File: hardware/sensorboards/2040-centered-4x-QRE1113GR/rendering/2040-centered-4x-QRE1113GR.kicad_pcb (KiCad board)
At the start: 2 copper layers, 174.6 x 52 mm, 44 parts, among them J1 Conn_01x10_Male, U1 QRE1113GR, U2 QRE1113GR, U3 QRE1113GR, U4 QRE1113GR

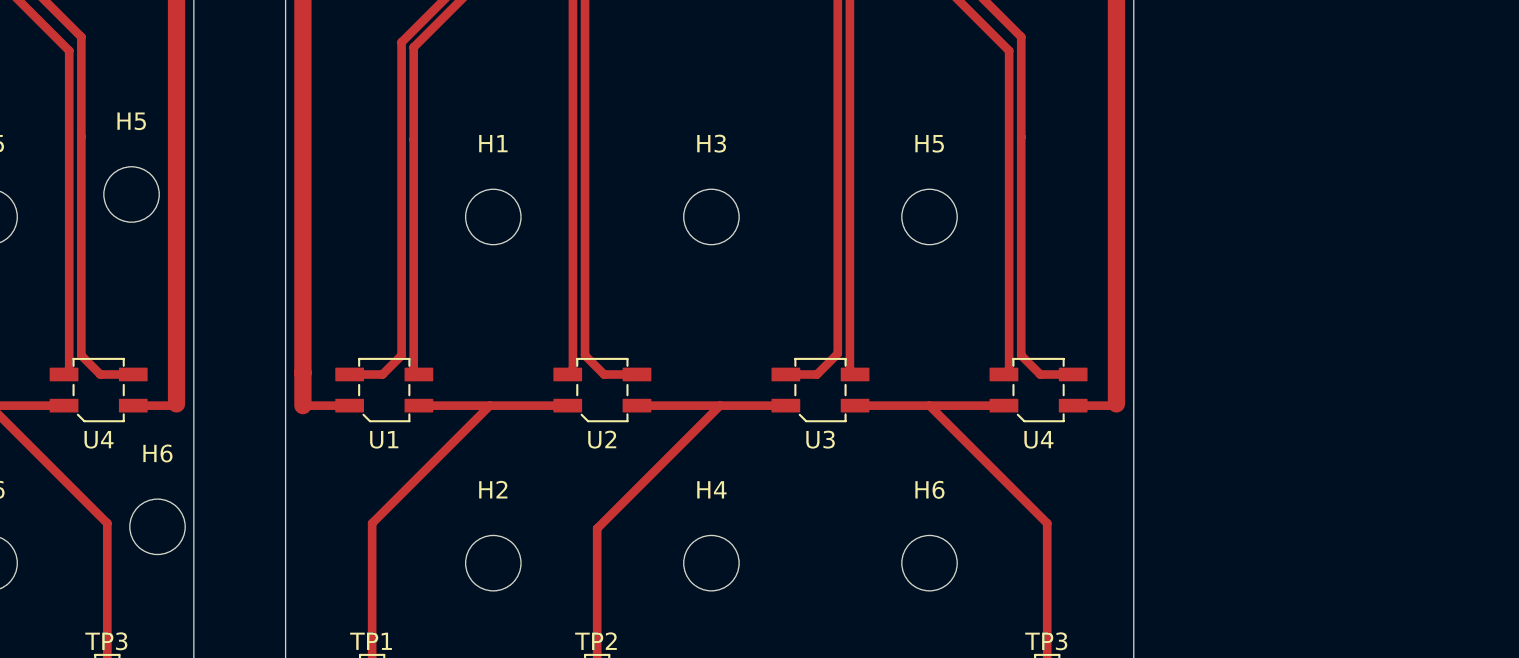
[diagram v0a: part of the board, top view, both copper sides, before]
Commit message: positioned screen and extrusions
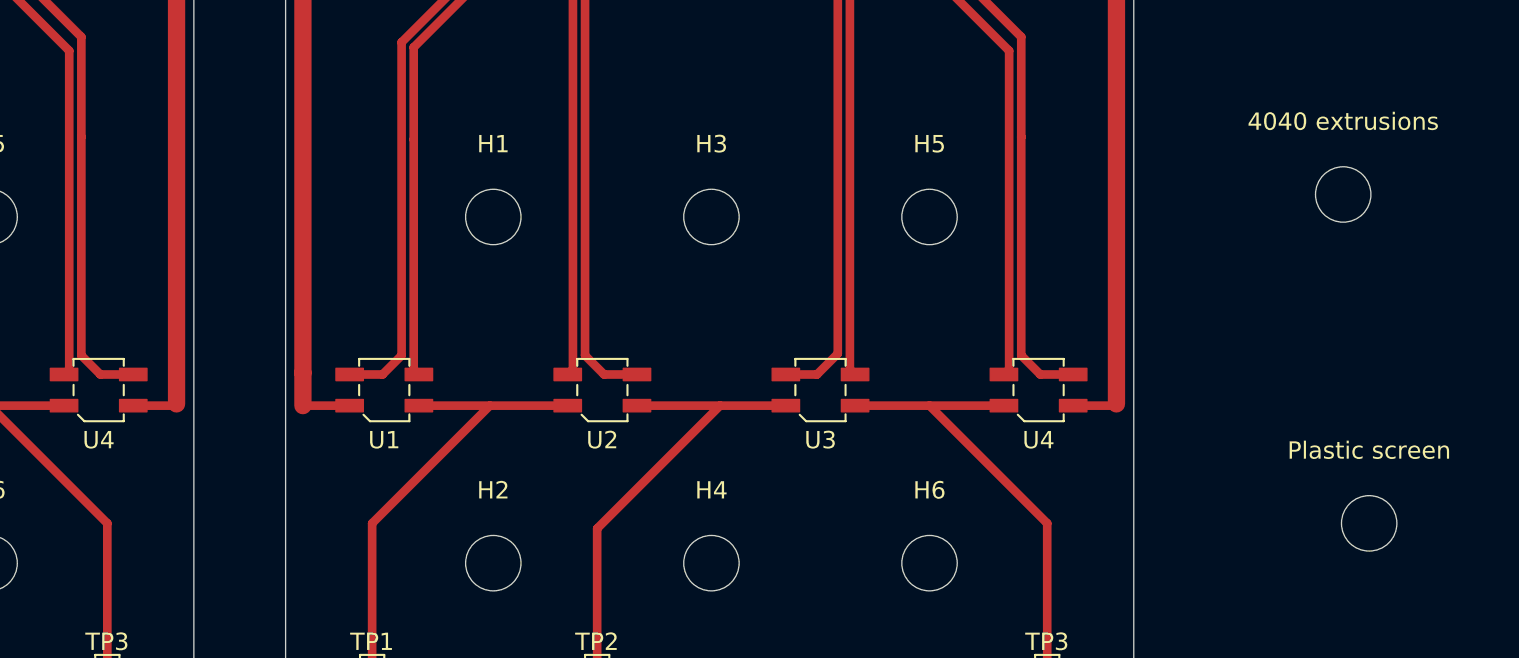
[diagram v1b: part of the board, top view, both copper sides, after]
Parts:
- 4040 extrusions: renamed from H5
- Plastic screen: renamed from H6
- moved Plastic screen 70.0 mm to (247.0, 100.0)
- moved 4040 extrusions 70.0 mm to (245.5, 81.0)
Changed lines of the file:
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@@
   )
   (footprint "Mounting_Holes:MountingHole_3.2mm_M3" (layer "F.Cu")
-    (at 177 100.2)
-    (descr "Mounting Hole 3.2mm, no annular, M3")
-    (tags "mounting hole 3.2mm no annular m3")
-    (property "Sheetfile" "2040-centered-4x-QRE1113GR.kicad_sch")
-    (property "Sheetname" "")
-    (attr exclude_from_pos_files)
-    (fp_text reference "H6" (at 0 -4.2) (layer "F.SilkS")
-      (effects (font (size 1 1) (thickness 0.15)))
-    )
-    (fp_text value "MountingHole" (at 0 4.2) (layer "F.Fab")
-      (effects (font (size 1 1) (thickness 0.15)))
-    )
-    (fp_text user "${REFERENCE}" (at 0 0) (layer "F.Fab")
+    (at 247 100)
+    (descr "Mounting Hole 3.2mm, no annular, M3")
+    (tags "mounting hole 3.2mm no annular m3")
+    (property "Sheetfile" "2040-centered-4x-QRE1113GR.kicad_sch")
+    (property "Sheetname" "")
+    (attr exclude_from_pos_files)
+    (fp_text reference "Plastic screen" (at 0 -4.2) (layer "F.SilkS")
+      (effects (font (size 1 1) (thickness 0.15)))
+    )
+    (fp_text value "MountingHole" (at 0 4.2) (layer "F.Fab")
       (effects (font (size 1 1) (thickness 0.15)))
     )
@@
     (pad "" np_thru_hole circle (at 0 0) (size 3.2 3.2) (drill 3.2) (layers *.Cu *.Mask))
     (model "${KIPRJMOD}/QRE1113-screen.wrl"
-      (offset (xyz -46.1 -12.2 0))
+      (offset (xyz -116.1 -11.7 0))
       (scale (xyz 0.39 0.39 0.39))
       (rotate (xyz 0 0 0))
@@
   )
   (footprint "Mounting_Holes:MountingHole_3.2mm_M3" (layer "F.Cu")
-    (at 175.5 81)
-    (descr "Mounting Hole 3.2mm, no annular, M3")
-    (tags "mounting hole 3.2mm no annular m3")
-    (property "Sheetfile" "2040-centered-4x-QRE1113GR.kicad_sch")
-    (property "Sheetname" "")
-    (attr exclude_from_pos_files)
-    (fp_text reference "H5" (at 0 -4.2) (layer "F.SilkS")
-      (effects (font (size 1 1) (thickness 0.15)))
-    )
-    (fp_text value "MountingHole" (at 0 4.2) (layer "F.Fab")
-      (effects (font (size 1 1) (thickness 0.15)))
-    )
-    (fp_text user "${REFERENCE}" (at 0 0) (layer "F.Fab")
+    (at 245.5 81)
+    (descr "Mounting Hole 3.2mm, no annular, M3")
+    (tags "mounting hole 3.2mm no annular m3")
+    (property "Sheetfile" "2040-centered-4x-QRE1113GR.kicad_sch")
+    (property "Sheetname" "")
+    (attr exclude_from_pos_files)
+    (fp_text reference "4040 extrusions" (at 0 -4.2) (layer "F.SilkS")
+      (effects (font (size 1 1) (thickness 0.15)))
+    )
+    (fp_text value "MountingHole" (at 0 4.2) (layer "F.Fab")
       (effects (font (size 1 1) (thickness 0.15)))
     )
@@
     (pad "" np_thru_hole circle (at 0 0) (size 3.2 3.2) (drill 3.2) (layers *.Cu *.Mask))
     (model "${KIPRJMOD}/HFSQN4-1050-500.igs"
-      (offset (xyz -55 -11 -13))
+      (offset (xyz -130 -11 -13))
       (scale (xyz 1 1 1))
       (rotate (xyz -90 0 90))
     )
     (model "${KIPRJMOD}/HFS5-4040-500.igs"
-      (offset (xyz -55 -11 -23))
+      (offset (xyz -125 -11 -23))
       (scale (xyz 1 1 1))
       (rotate (xyz -90 0 90))
